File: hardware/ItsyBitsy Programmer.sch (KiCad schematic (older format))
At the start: 19 parts

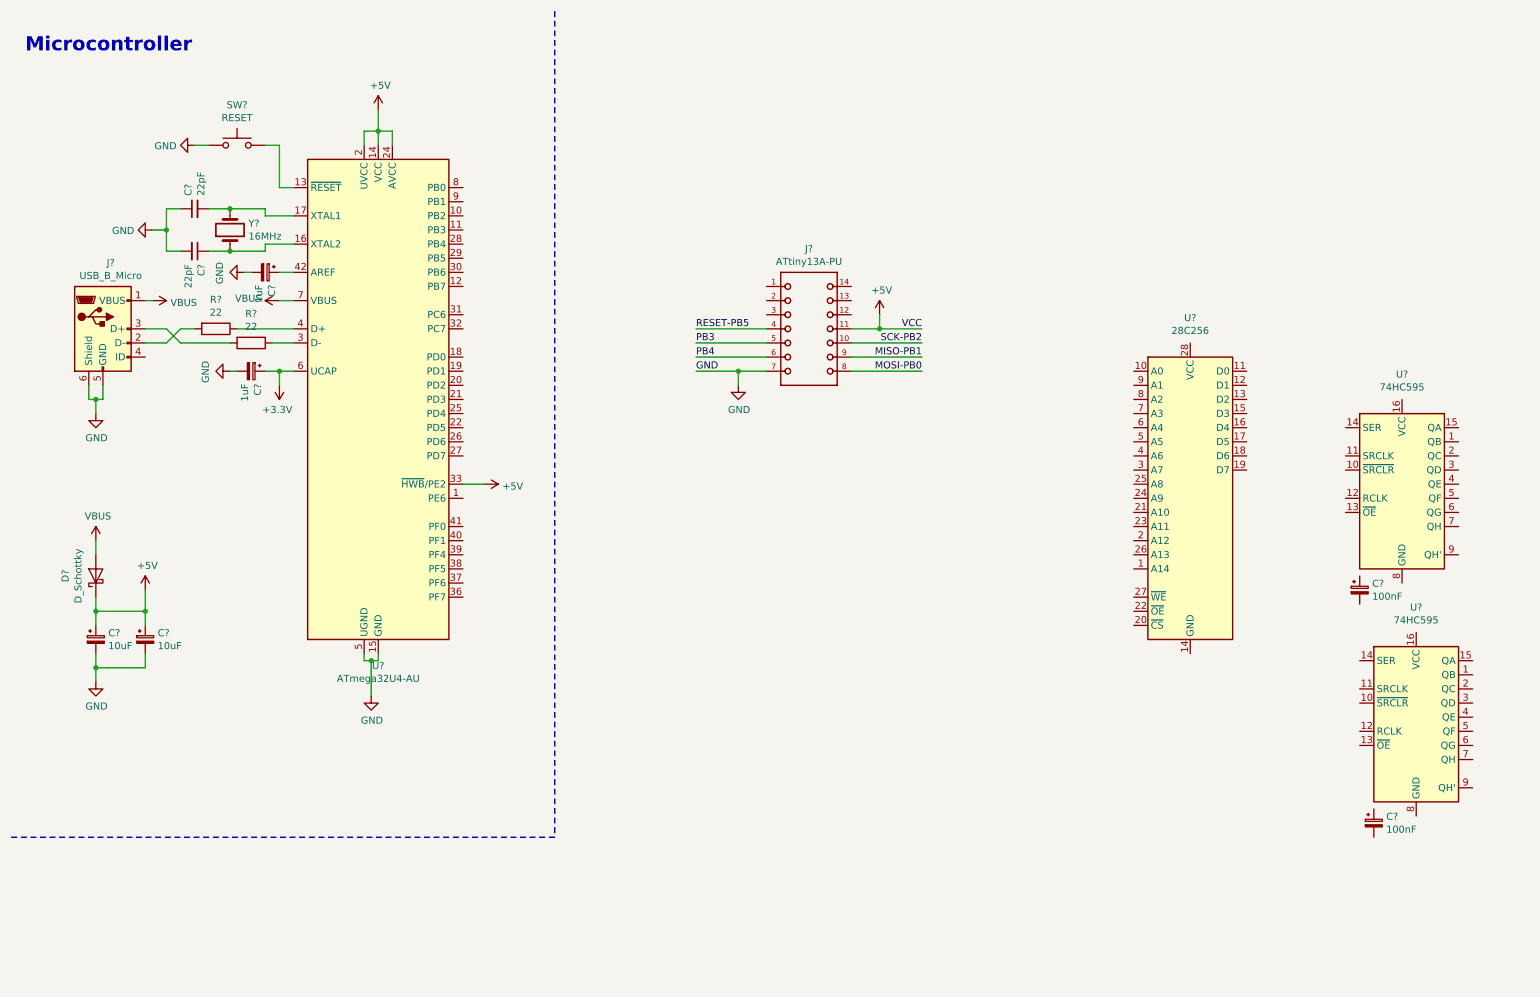
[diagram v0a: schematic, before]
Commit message: Hardware schematic updates. Need to work on power rails.
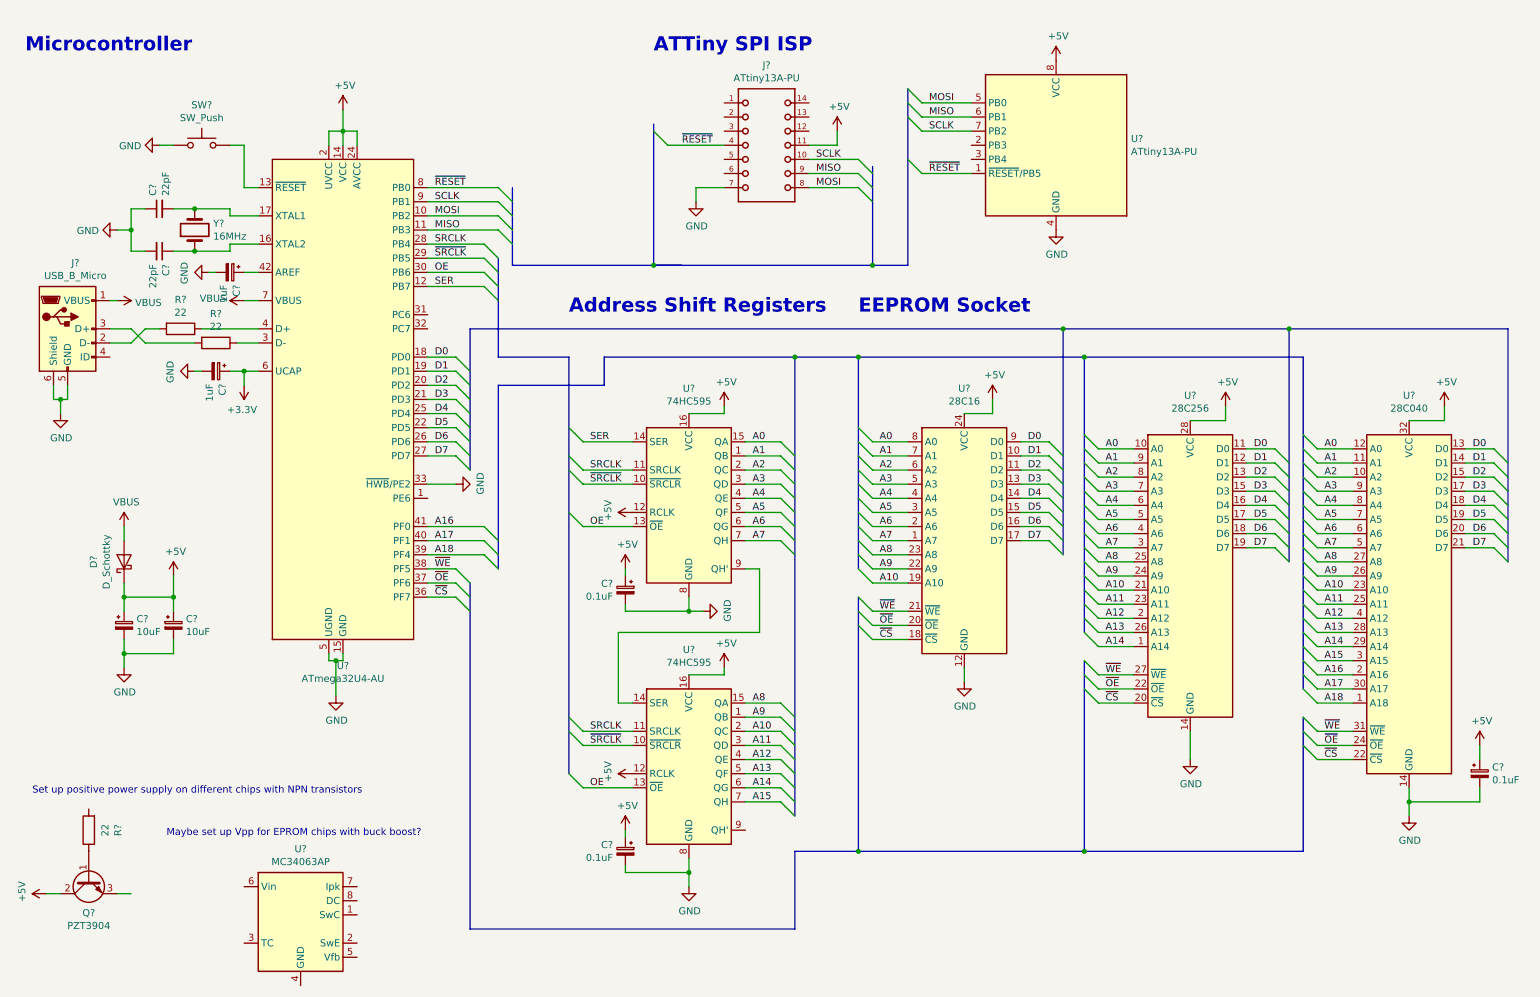
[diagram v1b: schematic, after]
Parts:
- removed C? (x2): 100nF, symbol Device:CP_Small
- removed SW?: RESET, symbol Switch:SW_Push
- removed U?: 28C256, symbol Memory_EEPROM:28C256
- removed U? (x2): 74HC595, symbol 74xx:74HC595
- added C? (x3): 0.1uF, symbol Device:CP_Small
- added Q?: PZT3904, Package_TO_SOT_SMD:SOT-223, symbol Transistor_BJT:PZT3904
- added R?: 22, symbol Device:R
- added SW?: SW_Push, symbol Switch:SW_Push
- added U? (x2): 74HC595, symbol 74xx:74HC595
- added U?: MC34063AP, Package_DIP:DIP-8_W7.62mm, symbol Regulator_Switching:MC34063AP
- added U?: ATtiny13A-PU, Package_DIP:DIP-8_W7.62mm, symbol MCU_Microchip_ATtiny:ATtiny13A-PU
- added U?: 28C256, symbol ItsyBitsy_EEPROM:28C256
- added U?: 28C16, symbol ItsyBitsy_EEPROM:28C16
- added U?: 28C040, symbol ItsyBitsy_EEPROM:28C040
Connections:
- net MISO-PB1 is gone; now on net MISO: J?.9
- net MOSI-PB0 is gone; now on net MOSI: J?.8
- net RESET-PB5 is gone; now on net ~RESET: J?.4
- net SCK-PB2 is gone; now on net SCLK: J?.10
- net +5V: now also C?.1, C?.1, C?.1, Q?.2 (C), Q?.4 (C), U?.12 (RCLK), U?.12 (RCLK), U?.16 (VCC), U?.16 (VCC), U?.24 (VCC), U?.28 (VCC), U?.32 (VCC), U?.8 (VCC); no longer U?.33 (~HWB~/PE2)
- net GND: now also U?.33 (~HWB~/PE2), C?.2, C?.2, C?.2, SW?.1, U?.12 (GND), U?.14 (GND), U?.14 (GND), U?.4 (GND), U?.8 (GND), U?.8 (GND)
- net MOSI: now reaches U?.10 (PB2)
- net MOSI: now also U?.5 (PB0)
- net MISO: now reaches U?.11 (PB3)
- net MISO: now also U?.6 (PB1)
- net SER: now reaches U?.12 (PB7)
- net SER: now also U?.14 (SER)
- net at U?.13 (~RESET): now also SW?.2
- net D0: now reaches U?.18 (PD0)
- net D0: now also U?.11 (D0), U?.13 (D0), U?.9 (D0)
- net D1: now reaches U?.19 (PD1)
- net D1: now also U?.10 (D1), U?.12 (D1), U?.14 (GND)
- net D2: now reaches U?.20 (PD2)
- net D2: now also U?.11 (D2), U?.13 (D2), U?.15 (D2)
- net D3: now reaches U?.21 (PD3)
- net D3: now also U?.13 (D3), U?.15 (D3), U?.17 (D3)
- net D5: now reaches U?.22 (PD5)
- net D5: now also U?.15 (D5), U?.17 (D5), U?.19 (D5)
- net D4: now reaches U?.25 (PD4)
- net D4: now also U?.14 (D4), U?.16 (D4), U?.18 (D4)
- net D6: now reaches U?.26 (PD6)
- net D6: now also U?.16 (D6), U?.18 (D6), U?.20 (D6)
- net D7: now reaches U?.27 (PD7)
- net D7: now also U?.17 (D7), U?.19 (D7), U?.21 (D7)
- net SRCLK: now reaches U?.28 (PB4)
- net SRCLK: now also U?.11 (SRCLK), U?.11 (SRCLK)
- net ~SRCLK: now reaches U?.29 (PB5)
- net ~SRCLK: now also U?.10 (~SRCLR), U?.10 (~SRCLR)
- net OE: now reaches U?.30 (PB6)
- net OE: now also U?.13 (~OE), U?.13 (~OE)
- net ~CS: now reaches U?.36 (PF7)
- net ~CS: now also U?.18 (~CS), U?.20 (~CS), U?.22 (~CS)
- net ~OE: now reaches U?.37 (PF6)
- net ~OE: now also U?.20 (~OE), U?.22 (~OE), U?.24 (~OE)
- net ~WE: now reaches U?.38 (PF5)
- net ~WE: now also U?.21 (~WE), U?.27 (~WE), U?.31 (~WE)
- net A18: now reaches U?.39 (PF4)
- net A18: now also U?.1 (A18)
- net A17: now reaches U?.40 (PF1)
- net A17: now also U?.30 (A17)
- net A16: now reaches U?.41 (PF0)
- net A16: now also U?.2 (A16)
- net ~RESET: now reaches U?.8 (PB0)
- net ~RESET: now also U?.1 (~RESET~/PB5)
- net SCLK: now reaches U?.9 (PB1)
- net SCLK: now also U?.7 (PB2)
- net PB3: no longer names the net of J?.5
- net PB4: no longer names the net of J?.6
- new net: Q?.1 (B), R?.1
- new net: U?.14 (SER), U?.9 (QH')
- new net A0: U?.10 (A0), U?.12 (A0), U?.15 (QA), U?.8 (A0)
- new net A1: U?.1 (QB), U?.11 (A1), U?.7 (A1), U?.9 (A1)
- new net A10: U?.19 (A10), U?.2 (QC), U?.21 (A10), U?.23 (A10)
- new net A11: U?.23 (A11), U?.25 (A11), U?.3 (QD)
- new net A12: U?.2 (A12), U?.4 (A12), U?.4 (QE)
- new net A13: U?.26 (A13), U?.28 (A13), U?.5 (QF)
- new net A14: U?.1 (A14), U?.29 (A14), U?.6 (QG)
- new net A15: U?.3 (A15), U?.7 (QH)
- new net A2: U?.10 (A2), U?.2 (QC), U?.6 (A2), U?.8 (A2)
- new net A3: U?.3 (QD), U?.5 (A3), U?.7 (A3), U?.9 (A3)
- new net A4: U?.4 (A4), U?.4 (QE), U?.6 (A4), U?.8 (A4)
- new net A5: U?.3 (A5), U?.5 (A5), U?.5 (QF), U?.7 (A5)
- new net A6: U?.2 (A6), U?.4 (A6), U?.6 (A6), U?.6 (QG)
- new net A7: U?.1 (A7), U?.3 (A7), U?.5 (A7), U?.7 (QH)
- new net A8: U?.15 (QA), U?.23 (A8), U?.25 (A8), U?.27 (A8)
- new net A9: U?.1 (QB), U?.22 (A9), U?.24 (A9), U?.26 (A9)
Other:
- note added: "ATTiny SPI ISP"
- note added: "Address Shift Registers"
- note added: "EEPROM Socket"
- note added: "Maybe set up Vpp for EPROM chips with buck boost?"
- note added: "Set up positive power supply on different chips with NPN transistors"
- moved on the sheet: C?, D?, J?, R?, U?, Y?
